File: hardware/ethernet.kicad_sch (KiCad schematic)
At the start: 37 parts, among them J701 J0011D21BNL, U701 W5500, U702 USBLC6-2P6, U703 USBLC6-2P6, Y701 25MHz

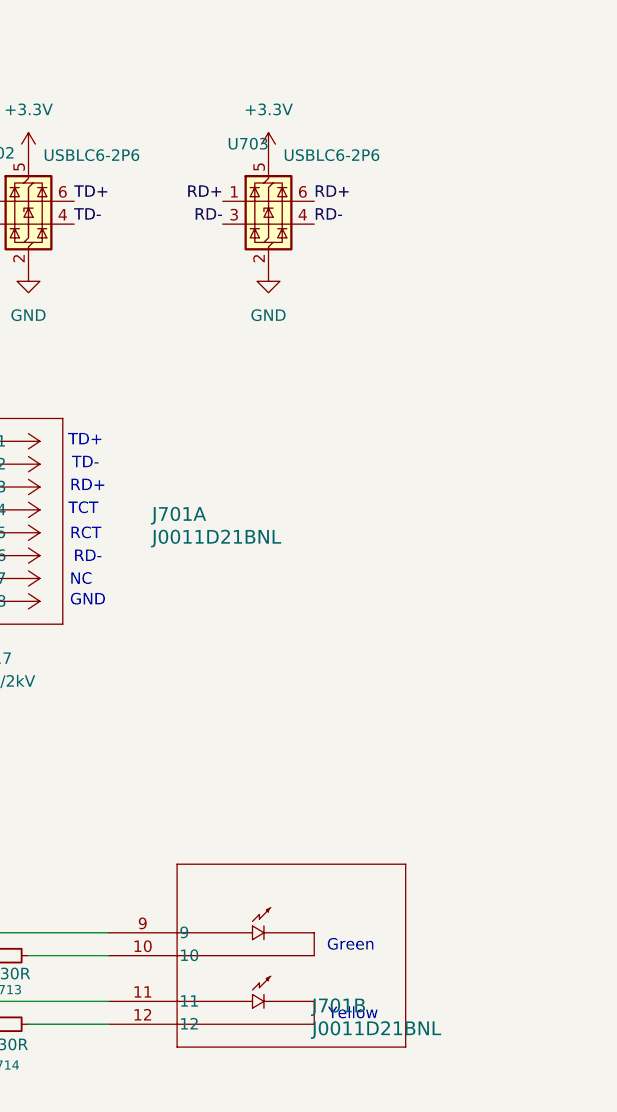
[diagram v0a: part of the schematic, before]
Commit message: added ship fet
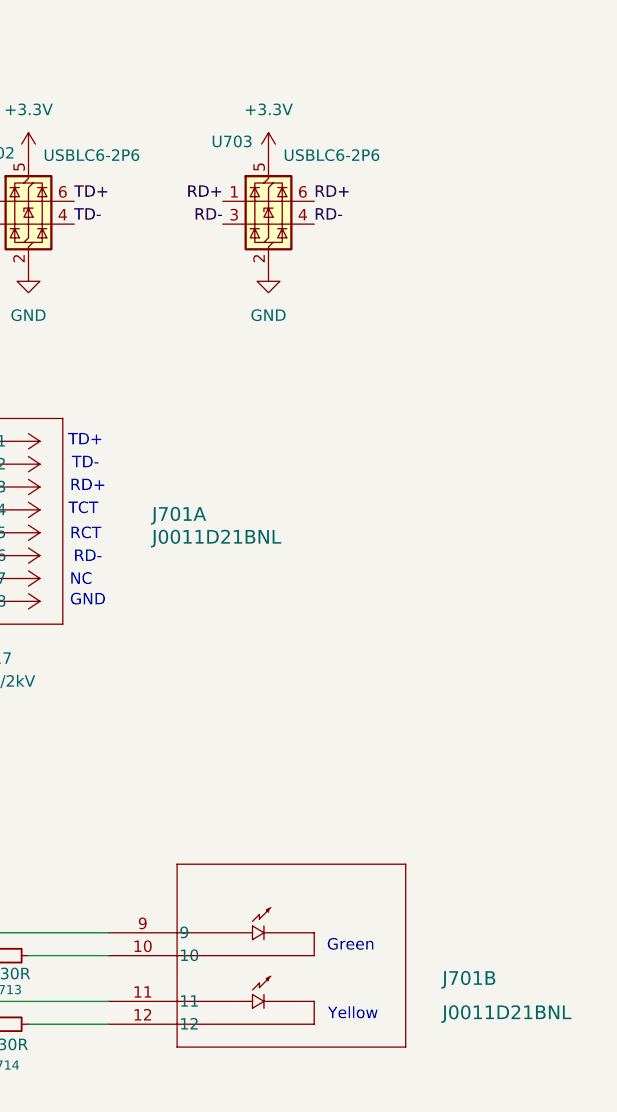
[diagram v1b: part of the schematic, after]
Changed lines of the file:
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@@
 		(dnp no)
 		(property "Reference" "U703"
-			(at 225.298 49.53 0)
+			(at 223.52 49.276 0)
 			(effects
 				(font
@@
 		(on_board yes)
 		(dnp no)
-		(fields_autoplaced yes)
 		(property "Reference" "J701"
-			(at 234.696 145.288 0)
+			(at 249.174 142.24 0)
 			(effects
 				(font
@@
 		)
 		(property "Value" "J0011D21BNL"
-			(at 234.696 147.828 0)
-			(effects
-				(font
+			(at 249.174 146.05 0)
+			(effects
+				(font

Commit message: footprint update
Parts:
- C701, C702, C703, C704, C705, C706, C707, C708, C709, C710, C711, C712, C713, C714, C715, C716, C717: footprint Capacitor_SMD:C_0402_1005Metric -> Capacitor_SMD:C_0805_2012Metric
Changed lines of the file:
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@@
 			)
 		)
-		(property "Footprint" "Capacitor_SMD:C_0402_1005Metric"
+		(property "Footprint" "Capacitor_SMD:C_0805_2012Metric"
 			(at 132.08 140.97 0)
 			(effects
@@
 			)
 		)
-		(property "Footprint" "Capacitor_SMD:C_0402_1005Metric"
+		(property "Footprint" "Capacitor_SMD:C_0805_2012Metric"
 			(at 73.66 53.34 0)
 			(effects
@@
 			)
 		)
-		(property "Footprint" "Capacitor_SMD:C_0402_1005Metric"
+		(property "Footprint" "Capacitor_SMD:C_0805_2012Metric"
 			(at 176.53 95.25 0)
 			(effects
@@
 			)
 		)
-		(property "Footprint" "Capacitor_SMD:C_0402_1005Metric"
+		(property "Footprint" "Capacitor_SMD:C_0805_2012Metric"
 			(at 121.92 140.97 0)
 			(effects
@@
 			)
 		)
-		(property "Footprint" "Capacitor_SMD:C_0402_1005Metric"
+		(property "Footprint" "Capacitor_SMD:C_0805_2012Metric"
 			(at 156.21 124.46 0)
 			(effects
@@
 			)
 		)
-		(property "Footprint" "Capacitor_SMD:C_0402_1005Metric"
+		(property "Footprint" "Capacitor_SMD:C_0805_2012Metric"
 			(at 57.15 137.16 0)
 			(effects
@@
 			)
 		)
-		(property "Footprint" "Capacitor_SMD:C_0402_1005Metric"
+		(property "Footprint" "Capacitor_SMD:C_0805_2012Metric"
 			(at 161.29 53.34 0)
 			(effects
@@
 			)
 		)
-		(property "Footprint" "Capacitor_SMD:C_0402_1005Metric"
+		(property "Footprint" "Capacitor_SMD:C_0805_2012Metric"
 			(at 165.1 109.22 0)
 			(effects
@@
 			)
 		)
-		(property "Footprint" "Capacitor_SMD:C_0402_1005Metric"
+		(property "Footprint" "Capacitor_SMD:C_0805_2012Metric"
 			(at 194.31 107.95 0)
 			(effects
@@
 			)
 		)
-		(property "Footprint" "Capacitor_SMD:C_0402_1005Metric"
+		(property "Footprint" "Capacitor_SMD:C_0805_2012Metric"
 			(at 151.13 53.34 0)
 			(effects
@@
 			)
 		)
-		(property "Footprint" "Capacitor_SMD:C_0402_1005Metric"
+		(property "Footprint" "Capacitor_SMD:C_0805_2012Metric"
 			(at 165.1 104.14 0)
 			(effects
@@
 			)
 		)
-		(property "Footprint" "Capacitor_SMD:C_0402_1005Metric"
+		(property "Footprint" "Capacitor_SMD:C_0805_2012Metric"
 			(at 140.97 53.34 0)
 			(effects
@@
 			)
 		)
-		(property "Footprint" "Capacitor_SMD:C_0402_1005Metric"
+		(property "Footprint" "Capacitor_SMD:C_0805_2012Metric"
 			(at 130.81 53.34 0)
 			(effects
@@
 			)
 		)
-		(property "Footprint" "Capacitor_SMD:C_0402_1005Metric"
+		(property "Footprint" "Capacitor_SMD:C_0805_2012Metric"
 			(at 110.49 53.34 0)
 			(effects
@@
 			)
 		)
-		(property "Footprint" "Capacitor_SMD:C_0402_1005Metric"
+		(property "Footprint" "Capacitor_SMD:C_0805_2012Metric"
 			(at 120.65 53.34 0)
 			(effects
@@
 			)
 		)
-		(property "Footprint" "Capacitor_SMD:C_0402_1005Metric"
+		(property "Footprint" "Capacitor_SMD:C_0805_2012Metric"
 			(at 83.82 53.34 0)
 			(effects
@@
 			)
 		)
-		(property "Footprint" "Capacitor_SMD:C_0402_1005Metric"
+		(property "Footprint" "Capacitor_SMD:C_0805_2012Metric"
 			(at 76.2 137.16 0)
 			(effects

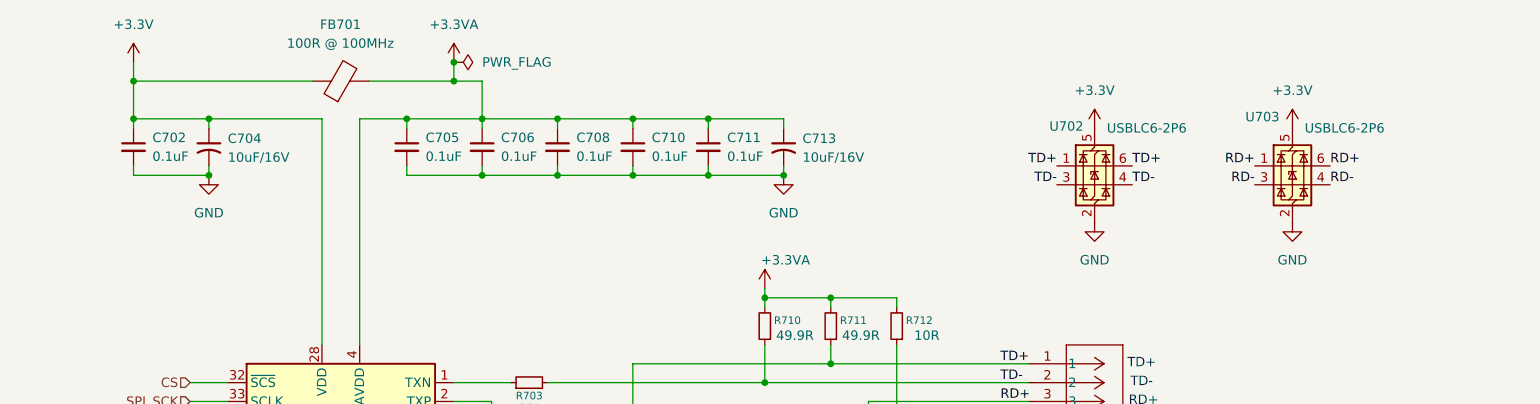
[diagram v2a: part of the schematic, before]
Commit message: updated ESD/Inductor footprints
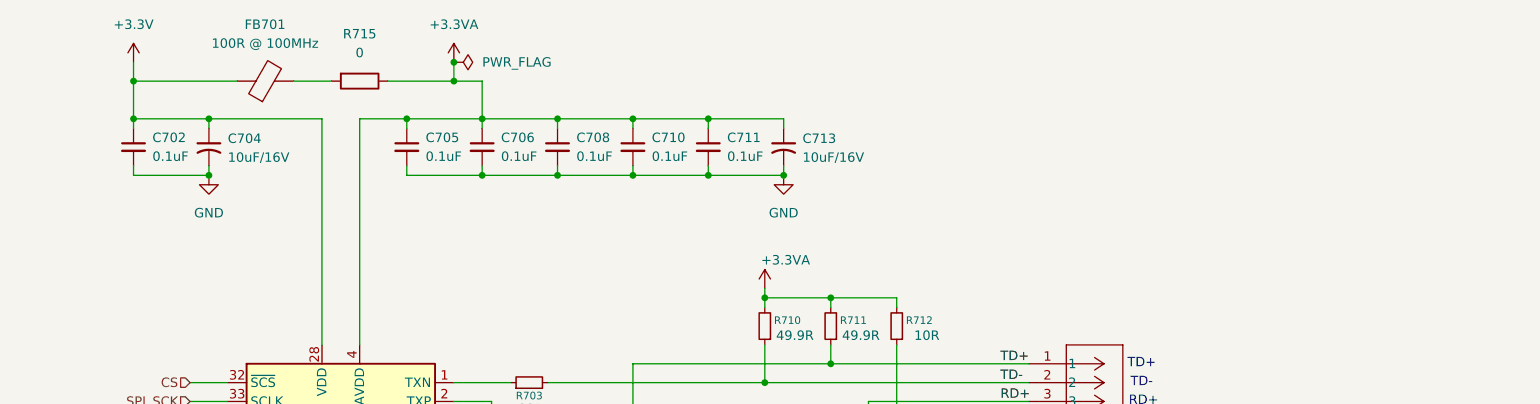
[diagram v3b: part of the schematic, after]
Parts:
- removed U702, U703: USBLC6-2P6, Package_TO_SOT_SMD:SOT-666, symbol Power_Protection:USBLC6-2P6
- added R715: 0, symbol Device:R
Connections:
- net +3.3VA: now also R715.1; no longer FB701.2
- new net: FB701.2, R715.2
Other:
- moved on the sheet: FB701

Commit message: pcb_update_1232
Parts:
- R715: footprint (none) -> Resistor_SMD:R_0805_2012Metric
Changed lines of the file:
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@@
 			)
 		)
-		(property "Footprint" ""
+		(property "Footprint" "Resistor_SMD:R_0805_2012Metric"
 			(at 104.14 42.672 90)
 			(effects

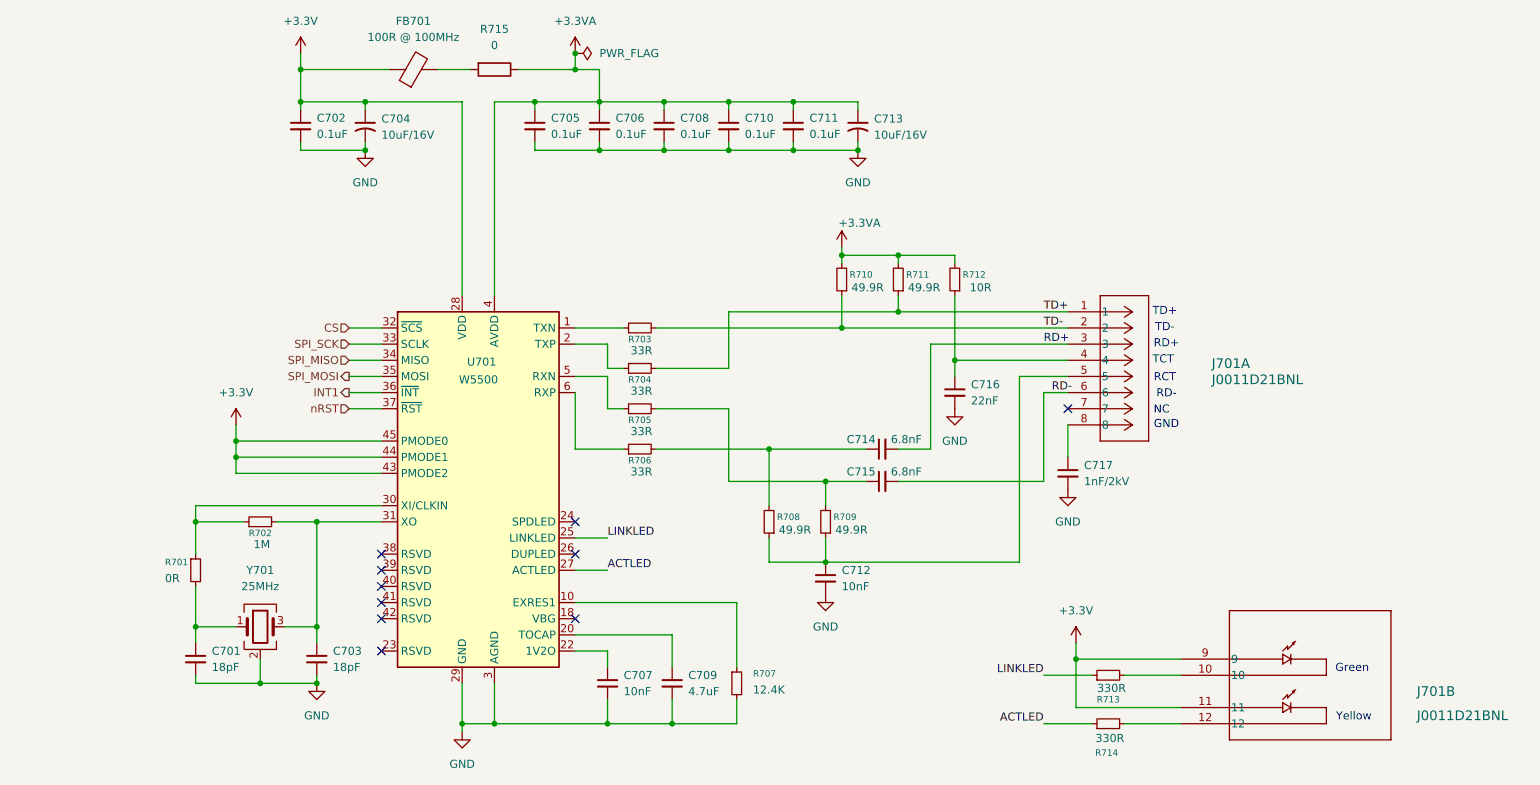
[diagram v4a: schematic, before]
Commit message: updated footprints
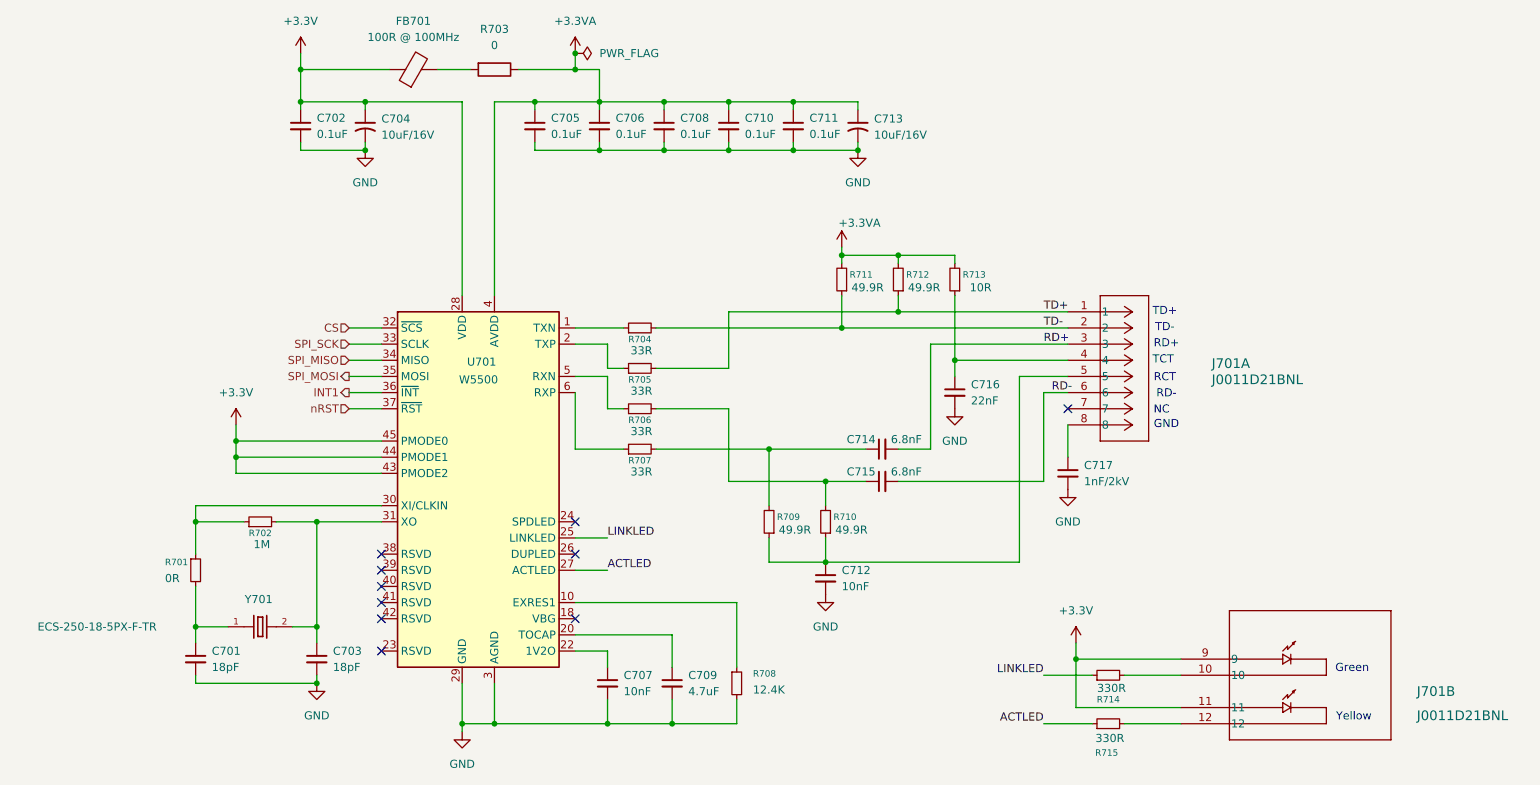
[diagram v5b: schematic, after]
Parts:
- removed Y701: 25MHz, Crystal:Crystal_SMD_3225-4Pin_3.2x2.5mm, symbol Device:Crystal_GND24
- added Y701: ECS-250-18-5PX-F-TR, pyronet_footprints:XTAL_ECS-250-18-5PX-F-TR, symbol pyronet_symbols:ECS-250-18-5PX-F-TR
- renumbered R715 to R703, R703 to R704, R704 to R705, R705 to R706, R706 to R707, R707 to R708, R708 to R709, R709 to R710, R710 to R711, R711 to R712, R712 to R713, R713 to R714, R714 to R715
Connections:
- net at C701.1, R701.2: now also Y701.1
- net at C703.1, R702.2, U701.31 (XO): now also Y701.2

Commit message: updated labels
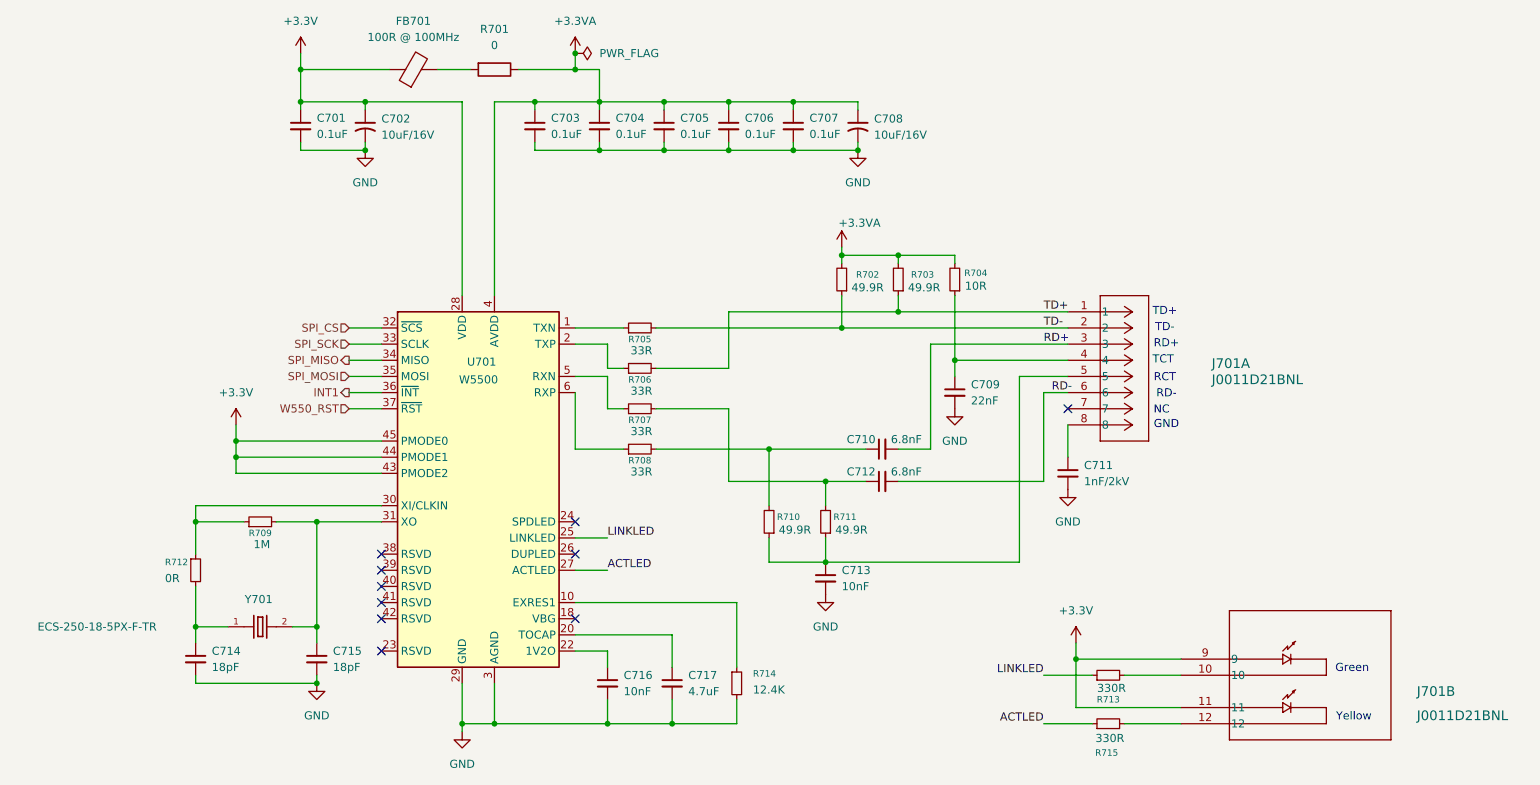
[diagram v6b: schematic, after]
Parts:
- renumbered C702 to C701, C704 to C702, C705 to C703, C706 to C704, C708 to C705, C710 to C706, C711 to C707, C713 to C708, C716 to C709, C714 to C710, C717 to C711, C715 to C712, C712 to C713, C701 to C714, C703 to C715, C707 to C716, C709 to C717, R703 to R701, R711 to R702, R712 to R703, R713 to R704, R704 to R705, R705 to R706, R706 to R707, R707 to R708, R702 to R709, R709 to R710, R710 to R711, R701 to R712, R714 to R713, R708 to R714
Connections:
- net CS renamed SPI_CS
- net nRST renamed W550_RST

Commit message: fixed ERC issues
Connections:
- net INT1 renamed W5500_INT
- net W550_RST renamed W5500_RST
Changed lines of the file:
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@@
 		)
 	)
-	(hierarchical_label "W550_RST"
+	(hierarchical_label "W5500_RST"
 		(shape input)
 		(at 81.28 97.79 180)
@@
 		)
 	)
-	(hierarchical_label "INT1"
+	(hierarchical_label "W5500_INT"
 		(shape output)
 		(at 81.28 95.25 180)

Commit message: reannotate
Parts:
- renumbered C701 to C601, C702 to C602, C703 to C603, C704 to C604, C705 to C605, C706 to C606, C707 to C607, C708 to C608, C709 to C609, C710 to C610, C711 to C611, C712 to C612, C713 to C613, C714 to C614, C715 to C615, C716 to C616, C717 to C617, FB701 to FB601, J701 to J601, R701 to R601, R702 to R602, R703 to R603, R704 to R604, R705 to R605, R706 to R606, R707 to R607, R708 to R608, R709 to R609, R710 to R610, R711 to R611, R712 to R612, R713 to R613, R714 to R614, R715 to R615, U701 to U601, Y701 to Y601
